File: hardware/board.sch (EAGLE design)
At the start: 47 parts, among them IC1 0915BM15A0001, J1 U.FL, U3 BLE113-A, X1 24MHz 8pF 10ppm -20C +70C, X3 MINI-USB-UX60-MB-5ST

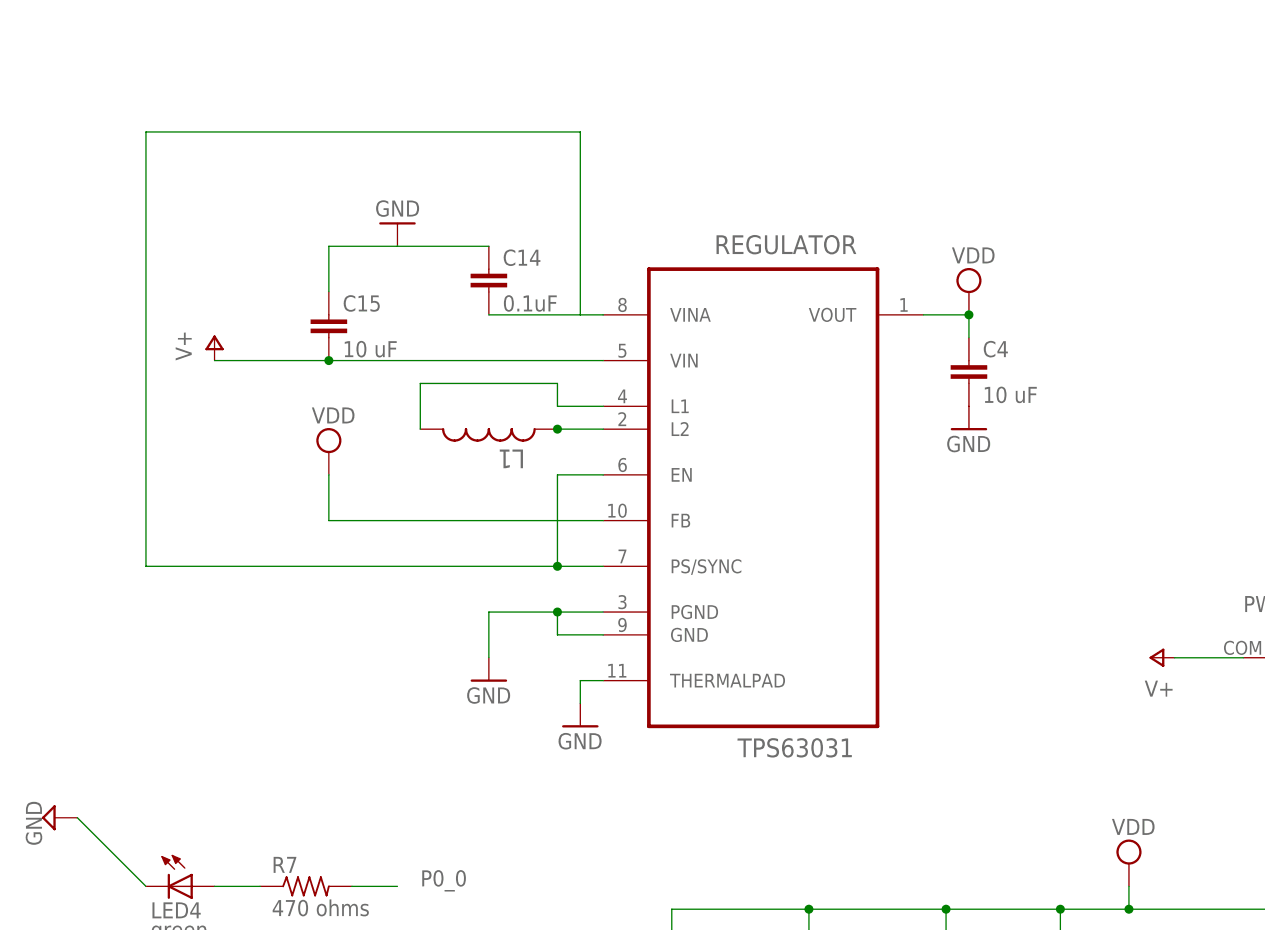
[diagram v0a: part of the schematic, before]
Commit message: Switch to buck-converter
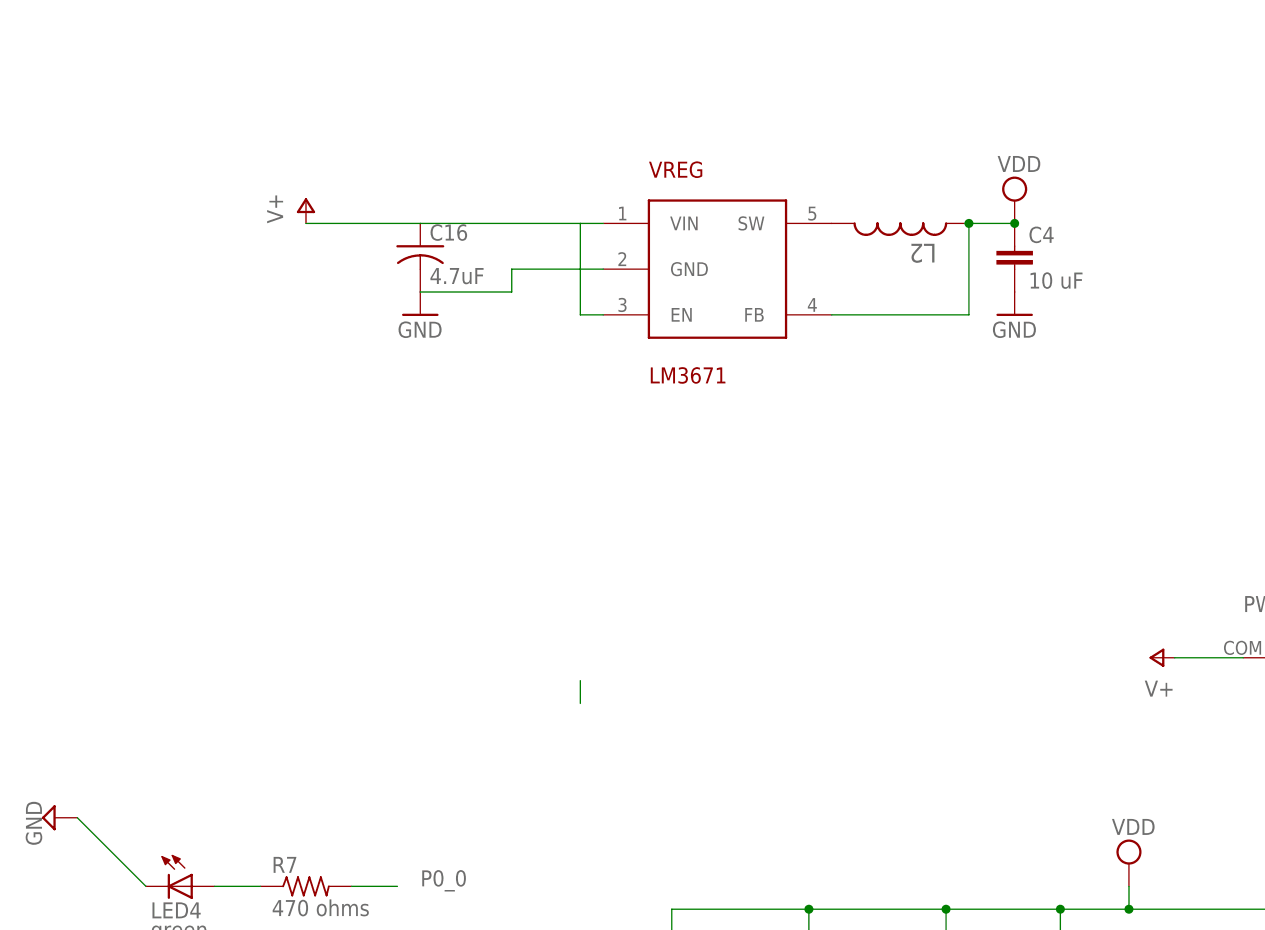
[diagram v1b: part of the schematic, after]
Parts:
- removed C14: 0.1uF, rcl:C-EUC0402
- removed C15: 10 uF, rcl:C-EUC0805K
- removed L1: 1.5 uH, rcl:L-USL2825P
- removed REGULATOR: TPS63031, board:TPS63031
- added C16: 4.7uF, rcl:C-USC0603K
- added L2: 2.2 uH, rcl:L-USL2825P
- added VREG: LM3671, texas-custom:LM3671
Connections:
- removed net N$1: L1.1, REGULATOR.L2
- removed net N$13: C14.2, REGULATOR.EN, REGULATOR.PS/SYNC, REGULATOR.VINA
- removed net N$6: L1.2, REGULATOR.L1
- new net N$16: L2.2, VREG.SW
- net GND: now also C16.2, VREG.GND; no longer C14.1, C15.1, REGULATOR.GND, REGULATOR.PGND, REGULATOR.THERMALPAD
- net V+: now also C16.1, VREG.EN, VREG.VIN; no longer C15.2, REGULATOR.VIN
- net VDD: now also L2.1, VREG.FB; no longer REGULATOR.FB, REGULATOR.VOUT
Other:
- moved on the sheet: C4

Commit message: Add partnames to pcb, and update bom
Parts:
- renumbered C16 to C14, JP2 to ALT.PWR, L2 to L1
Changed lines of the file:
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@@
 <part name="FID2" library="adafruit" deviceset="FIDUCIAL" device=""/>
 <part name="FID3" library="adafruit" deviceset="FIDUCIAL" device=""/>
-<part name="JP2" library="pinhead" deviceset="PINHD-1X2" device=""/>
+<part name="ALT.PWR" library="pinhead" deviceset="PINHD-1X2" device=""/>
 <part name="GND12" library="supply1" deviceset="GND" device=""/>
 <part name="VREG" library="texas-custom" deviceset="LM3671" device=""/>
 <part name="GND21" library="supply1" deviceset="GND" device=""/>
-<part name="C16" library="rcl" deviceset="C-US" device="C0603K" value="4.7uF"/>
+<part name="C14" library="rcl" deviceset="C-US" device="C0603K" value="4.7uF"/>
 <part name="P+3" library="supply1" deviceset="V+" device=""/>
-<part name="L2" library="rcl" deviceset="L-US" device="L2825P" value="2.2 uH"/>
+<part name="L1" library="rcl" deviceset="L-US" device="L2825P" value="2.2 uH"/>
 </parts>
 <sheets>
@@
 <instance part="FID2" gate="G$1" x="132.08" y="-50.8"/>
 <instance part="FID3" gate="G$1" x="147.32" y="-50.8"/>
-<instance part="JP2" gate="G$1" x="152.4" y="190.5"/>
+<instance part="ALT.PWR" gate="G$1" x="152.4" y="190.5"/>
 <instance part="GND12" gate="1" x="134.62" y="195.58" rot="R180"/>
 <instance part="VREG" gate="G$1" x="27.94" y="177.8"/>
 <instance part="GND21" gate="1" x="-5.08" y="172.72"/>
-<instance part="C16" gate="G$1" x="-5.08" y="180.34"/>
+<instance part="C14" gate="G$1" x="-5.08" y="180.34"/>
 <instance part="P+3" gate="1" x="-17.78" y="185.42"/>
-<instance part="L2" gate="G$1" x="48.26" y="182.88" smashed="yes" rot="R270">
+<instance part="L1" gate="G$1" x="48.26" y="182.88" smashed="yes" rot="R270">
 <attribute name="NAME" x="52.2986" y="180.6194" size="2.0828" layer="95" ratio="10" rot="SR180"/>
 </instance>
@@
 </segment>
 <segment>
-<pinref part="JP2" gate="G$1" pin="1"/>
+<pinref part="ALT.PWR" gate="G$1" pin="1"/>
 <pinref part="GND12" gate="1" pin="GND"/>
 <wire x1="149.86" y1="193.04" x2="134.62" y2="193.04" width="0.1524" layer="91"/>
 </segment>
 <segment>
-<pinref part="C16" gate="G$1" pin="2"/>
+<pinref part="C14" gate="G$1" pin="2"/>
 <pinref part="GND21" gate="1" pin="GND"/>
 <pinref part="VREG" gate="G$1" pin="GND"/>
@@
 <pinref part="C4" gate="G$1" pin="1"/>
 <pinref part="SUPPLY2" gate="G$1" pin="VDD"/>
-<pinref part="L2" gate="G$1" pin="1"/>
+<pinref part="L1" gate="G$1" pin="1"/>
 <junction x="55.88" y="182.88"/>
-<pinref part="L2" gate="G$1" pin="1"/>
+<pinref part="L1" gate="G$1" pin="1"/>
 <wire x1="55.88" y1="182.88" x2="60.96" y2="182.88" width="0.1524" layer="91"/>
 <junction x="60.96" y="182.88"/>
@@
 <wire x1="142.24" y1="182.88" x2="175.26" y2="182.88" width="0.1524" layer="91"/>
 <wire x1="142.24" y1="182.88" x2="142.24" y2="190.5" width="0.1524" layer="91"/>
-<pinref part="JP2" gate="G$1" pin="2"/>
+<pinref part="ALT.PWR" gate="G$1" pin="2"/>
 <wire x1="142.24" y1="190.5" x2="149.86" y2="190.5" width="0.1524" layer="91"/>
 </segment>
@@
 <segment>
 <pinref part="VREG" gate="G$1" pin="VIN"/>
-<pinref part="C16" gate="G$1" pin="1"/>
+<pinref part="C14" gate="G$1" pin="1"/>
 <wire x1="15.24" y1="182.88" x2="12.7" y2="182.88" width="0.1524" layer="91"/>
 <pinref part="VREG" gate="G$1" pin="EN"/>
@@
 <segment>
 <pinref part="VREG" gate="G$1" pin="SW"/>
-<pinref part="L2" gate="G$1" pin="2"/>
-</segment>
-</net>
+<pinref part="L1" gate="G$1" pin="2"/>
+</segment>
+</net>

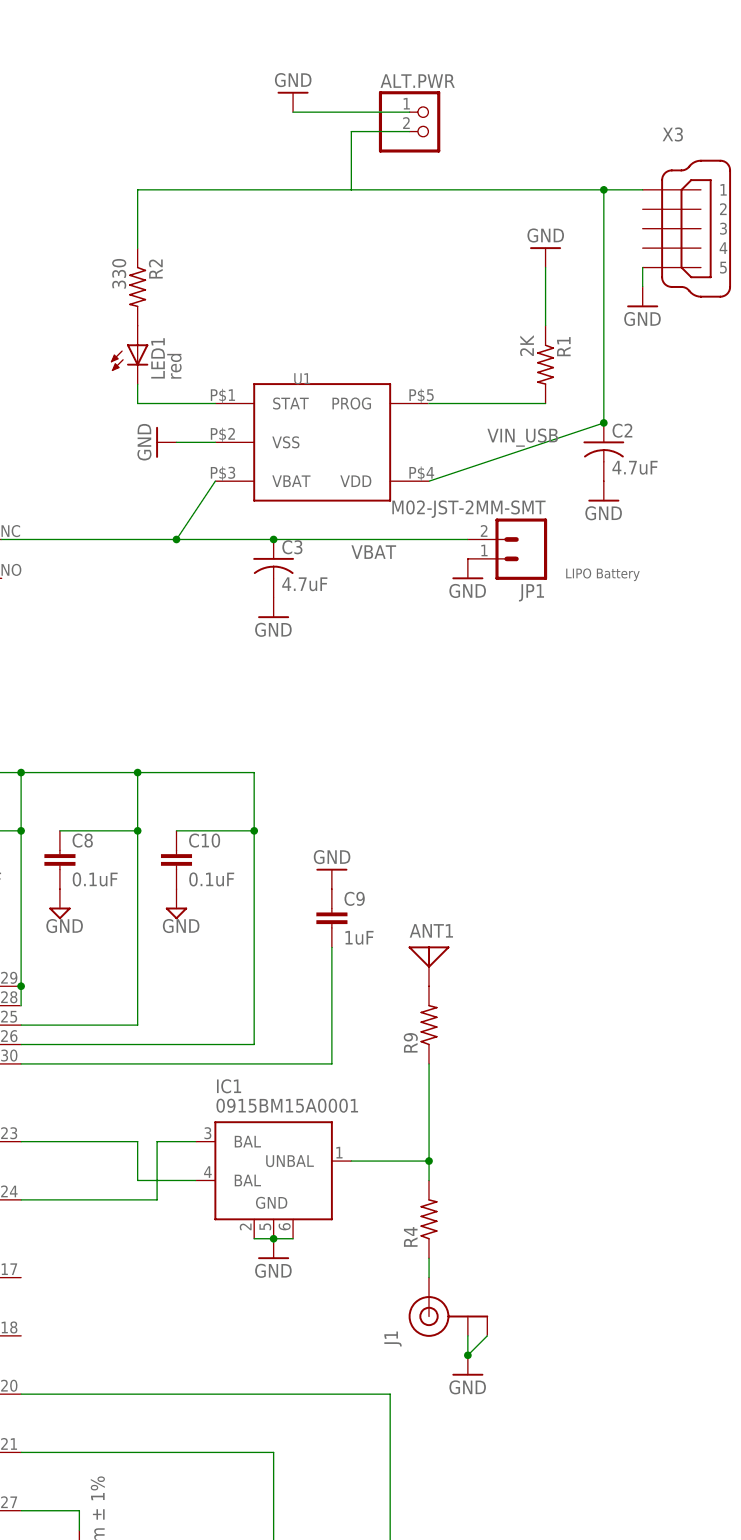
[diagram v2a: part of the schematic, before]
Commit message: Expand clear area around antenna; remove unused u.FL and AUX.PWR connectors.
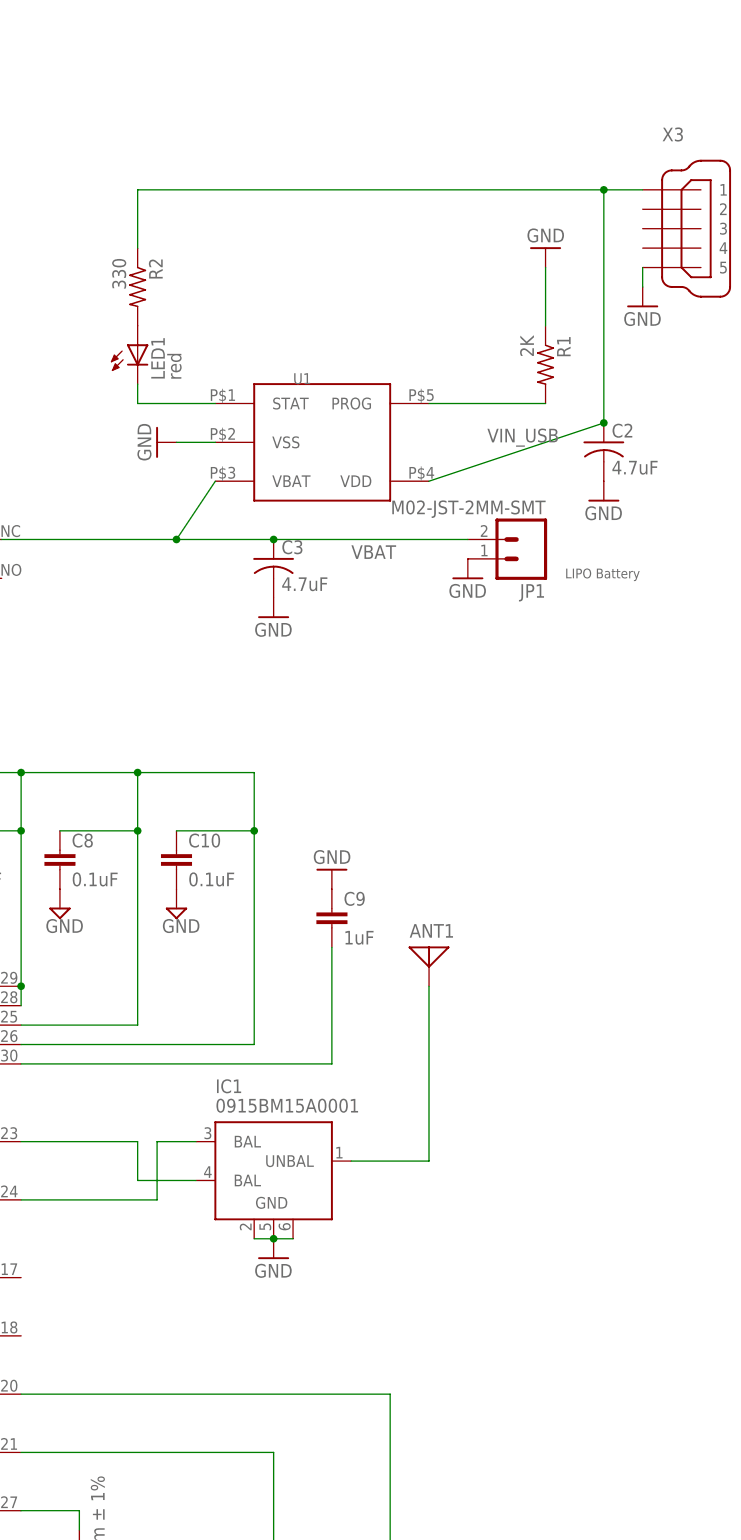
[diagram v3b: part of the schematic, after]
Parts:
- removed ALT.PWR: (no value), pinhead:PINHD-1X2
- removed J1: U.FL, SparkFun-Connectors:U.FL
- removed R4, R9: (no value), rcl:R-US_R0402
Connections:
- removed net N$12: ANT1.1, R9.2
- removed net N$9: J1.SIGNAL, R4.1
- net GND: no longer ALT.PWR.1, J1.GND@0, J1.GND@1
- net N$10: now also ANT1.1; no longer R4.2, R9.1
- net VIN_USB: no longer ALT.PWR.2
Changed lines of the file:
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@@
 <part name="SUPPLY2" library="supply2" deviceset="VDD" device=""/>
 <part name="SUPPLY5" library="supply2" deviceset="GND" device=""/>
-<part name="J1" library="SparkFun-Connectors" deviceset="U.FL" device="" value="U.FL"/>
 <part name="U3" library="sf-bluegiga" deviceset="BLE113" device="-A"/>
 <part name="C5" library="rcl" deviceset="C-EU" device="C0402K" value="12pF ±5%"/>
@@
 <part name="IC1" library="parts" deviceset="0915BM15A0001" device=""/>
 <part name="GND10" library="supply1" deviceset="GND" device=""/>
-<part name="R4" library="rcl" deviceset="R-US_" device="R0402"/>
 <part name="ANT1" library="discrete" deviceset="ANTENNA" device=""/>
-<part name="R9" library="rcl" deviceset="R-US_" device="R0402"/>
 <part name="CC1110-DEBUG" library="parts" deviceset="CC-DEBUG-PWR" device=""/>
 <part name="BLE113-DEBUG" library="parts" deviceset="CC-DEBUG-PWR" device=""/>
@@
 <part name="SUPPLY15" library="supply2" deviceset="GND" device=""/>
 <part name="SUPPLY18" library="supply2" deviceset="VDD" device=""/>
-<part name="GND20" library="supply1" deviceset="GND" device=""/>
 <part name="FID1" library="adafruit" deviceset="FIDUCIAL" device=""/>
 <part name="FID2" library="adafruit" deviceset="FIDUCIAL" device=""/>
 <part name="FID3" library="adafruit" deviceset="FIDUCIAL" device=""/>
-<part name="ALT.PWR" library="pinhead" deviceset="PINHD-1X2" device=""/>
-<part name="GND12" library="supply1" deviceset="GND" device=""/>
 <part name="VREG" library="texas-custom" deviceset="LM3671" device=""/>
 <part name="GND21" library="supply1" deviceset="GND" device=""/>
@@
 <instance part="SUPPLY2" gate="G$1" x="60.96" y="185.42"/>
 <instance part="SUPPLY5" gate="GND" x="76.2" y="-2.54"/>
-<instance part="J1" gate="G$1" x="152.4" y="35.56" rot="R90"/>
 <instance part="U3" gate="G$1" x="60.96" y="-48.26" rot="MR180"/>
 <instance part="C5" gate="G$1" x="147.32" y="-17.78"/>
@@
 <instance part="IC1" gate="G$1" x="132.08" y="53.34"/>
 <instance part="GND10" gate="1" x="132.08" y="43.18"/>
-<instance part="R4" gate="G$1" x="152.4" y="48.26" rot="R90"/>
 <instance part="ANT1" gate="A" x="152.4" y="83.82"/>
-<instance part="R9" gate="G$1" x="152.4" y="73.66" rot="R90"/>
 <instance part="CC1110-DEBUG" gate="G$1" x="-17.78" y="55.88" rot="R180"/>
 <instance part="BLE113-DEBUG" gate="G$1" x="-15.24" y="-15.24" rot="R180"/>
@@
 <instance part="SUPPLY15" gate="GND" x="66.04" y="93.98"/>
 <instance part="SUPPLY18" gate="G$1" x="22.86" y="-68.58" rot="R180"/>
-<instance part="GND20" gate="1" x="157.48" y="27.94"/>
 <instance part="FID1" gate="G$1" x="111.76" y="-50.8"/>
 <instance part="FID2" gate="G$1" x="132.08" y="-50.8"/>
 <instance part="FID3" gate="G$1" x="147.32" y="-50.8"/>
-<instance part="ALT.PWR" gate="G$1" x="152.4" y="190.5"/>
-<instance part="GND12" gate="1" x="134.62" y="195.58" rot="R180"/>
 <instance part="VREG" gate="G$1" x="27.94" y="177.8"/>
 <instance part="GND21" gate="1" x="-5.08" y="172.72"/>
@@
 <pinref part="C11" gate="G$1" pin="2"/>
 <pinref part="SUPPLY15" gate="GND" pin="GND"/>
-</segment>
-<segment>
-<pinref part="J1" gate="G$1" pin="GND@0"/>
-<pinref part="J1" gate="G$1" pin="GND@1"/>
-<wire x1="157.48" y1="30.48" x2="160.02" y2="33.02" width="0.1524" layer="91"/>
-<pinref part="GND20" gate="1" pin="GND"/>
-<junction x="157.48" y="30.48"/>
-<wire x1="157.48" y1="30.48" x2="157.48" y2="33.02" width="0.1524" layer="91"/>
-</segment>
-<segment>
-<pinref part="ALT.PWR" gate="G$1" pin="1"/>
-<pinref part="GND12" gate="1" pin="GND"/>
-<wire x1="149.86" y1="193.04" x2="134.62" y2="193.04" width="0.1524" layer="91"/>
 </segment>
 <segment>
@@
 <pinref part="R2" gate="G$1" pin="1"/>
 <wire x1="114.3" y1="175.26" x2="114.3" y2="182.88" width="0.1524" layer="91"/>
-<wire x1="114.3" y1="182.88" x2="142.24" y2="182.88" width="0.1524" layer="91"/>
 <junction x="175.26" y="182.88"/>
-<wire x1="142.24" y1="182.88" x2="175.26" y2="182.88" width="0.1524" layer="91"/>
-<wire x1="142.24" y1="182.88" x2="142.24" y2="190.5" width="0.1524" layer="91"/>
-<pinref part="ALT.PWR" gate="G$1" pin="2"/>
-<wire x1="142.24" y1="190.5" x2="149.86" y2="190.5" width="0.1524" layer="91"/>
+<wire x1="114.3" y1="182.88" x2="175.26" y2="182.88" width="0.1524" layer="91"/>
 </segment>
 </net>
@@
 </segment>
 </net>
-<net name="N$9" class="0">
-<segment>
-<pinref part="J1" gate="G$1" pin="SIGNAL"/>
-<pinref part="R4" gate="G$1" pin="1"/>
-<wire x1="152.4" y1="43.18" x2="152.4" y2="40.64" width="0.1524" layer="91"/>
-</segment>
-</net>
 <net name="N$10" class="0">
 <segment>
-<pinref part="R4" gate="G$1" pin="2"/>
-<wire x1="152.4" y1="53.34" x2="152.4" y2="55.88" width="0.1524" layer="91"/>
 <pinref part="IC1" gate="G$1" pin="UNBAL"/>
 <wire x1="142.24" y1="55.88" x2="152.4" y2="55.88" width="0.1524" layer="91"/>
-<junction x="152.4" y="55.88"/>
-<pinref part="R9" gate="G$1" pin="1"/>
-<wire x1="152.4" y1="55.88" x2="152.4" y2="68.58" width="0.1524" layer="91"/>
-</segment>
-</net>
-<net name="N$12" class="0">
-<segment>
+<wire x1="152.4" y1="55.88" x2="152.4" y2="78.74" width="0.1524" layer="91"/>
 <pinref part="ANT1" gate="A" pin="1"/>
-<pinref part="R9" gate="G$1" pin="2"/>
-</segment>
-</net>
+</segment>
+</net>
